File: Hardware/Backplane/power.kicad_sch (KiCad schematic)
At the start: 59 parts, among them J2901 Conn_01x05, U2901 P2X8C4M64P, U2902 AP3445LW6-7

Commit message: Adjusts to review comments
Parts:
- C2901: footprint (none) -> Capacitor_SMD:C_1206_3216Metric; Digikey Part No (none) -> 490-13970-1-ND
- C2902, C2903, C2904, C2905, C2906, C2907, C2908, C2909, C2910, C2911, C2912, C2913, C2914, C2915, C2916, C2917, C2918, C2919, C2920, C2921, C2922, C2923, C2924, C2925, C2926, C2927, C2928, C2929, C2930, C2931, C2932, C2933, C2934: Digikey Part No (none) -> 399-C0603C104M4RACTUCT-ND
- C2935: footprint (none) -> Capacitor_SMD:C_0603_1608Metric; Digikey Part No (none) -> 1276-1070-1-ND
- C2936, C2937: footprint (none) -> Capacitor_SMD:C_0603_1608Metric; Digikey Part No (none) -> 1276-1274-1-ND
- F2901, F2902, F2903: value SMD1206B050TF/15 -> 0ZCF0400FF2A; footprint (none) -> Fuse:Fuse_2920_7451Metric; Digikey Part No 13-SMD1206B050TF/15TR-ND -> 5923-0ZCF0400FF2ACT-ND
- R2901: Digikey Part No (none) -> RR08P75.0KDCT-ND
- R2902: Digikey Part No (none) -> P36KDBCT-ND
- R2903, R2904, R2905, R2906: Digikey Part No (none) -> 311-0.0GRCT-ND

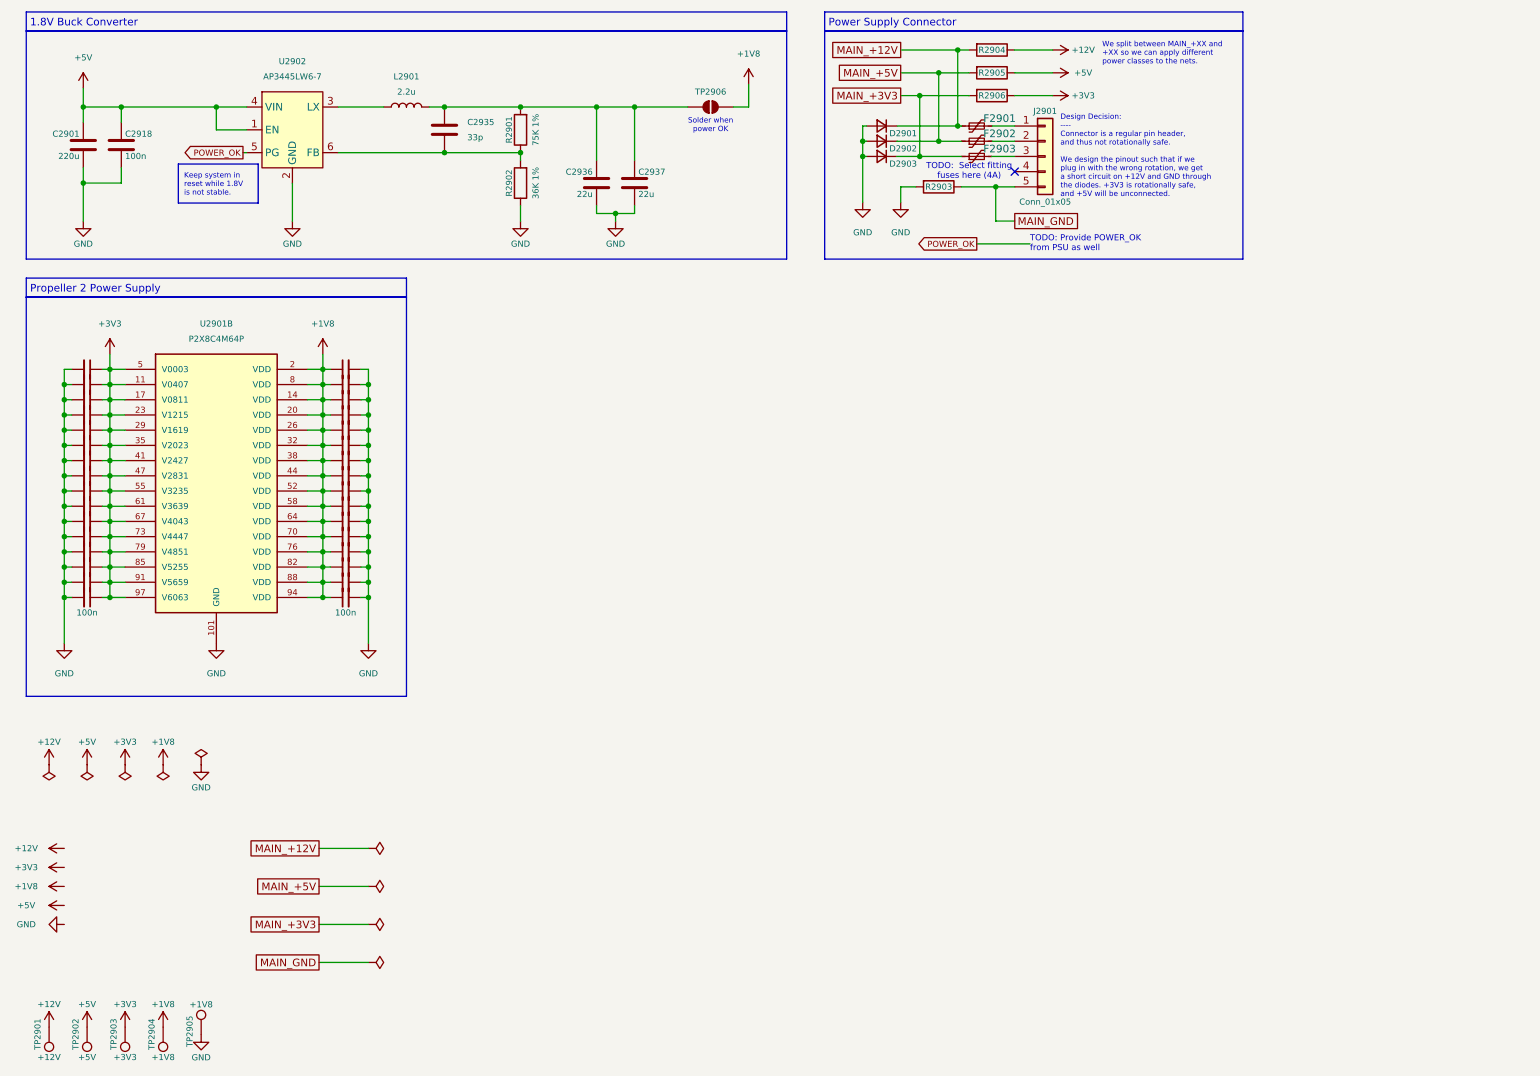
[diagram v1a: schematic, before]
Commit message: Cleans up power connector.
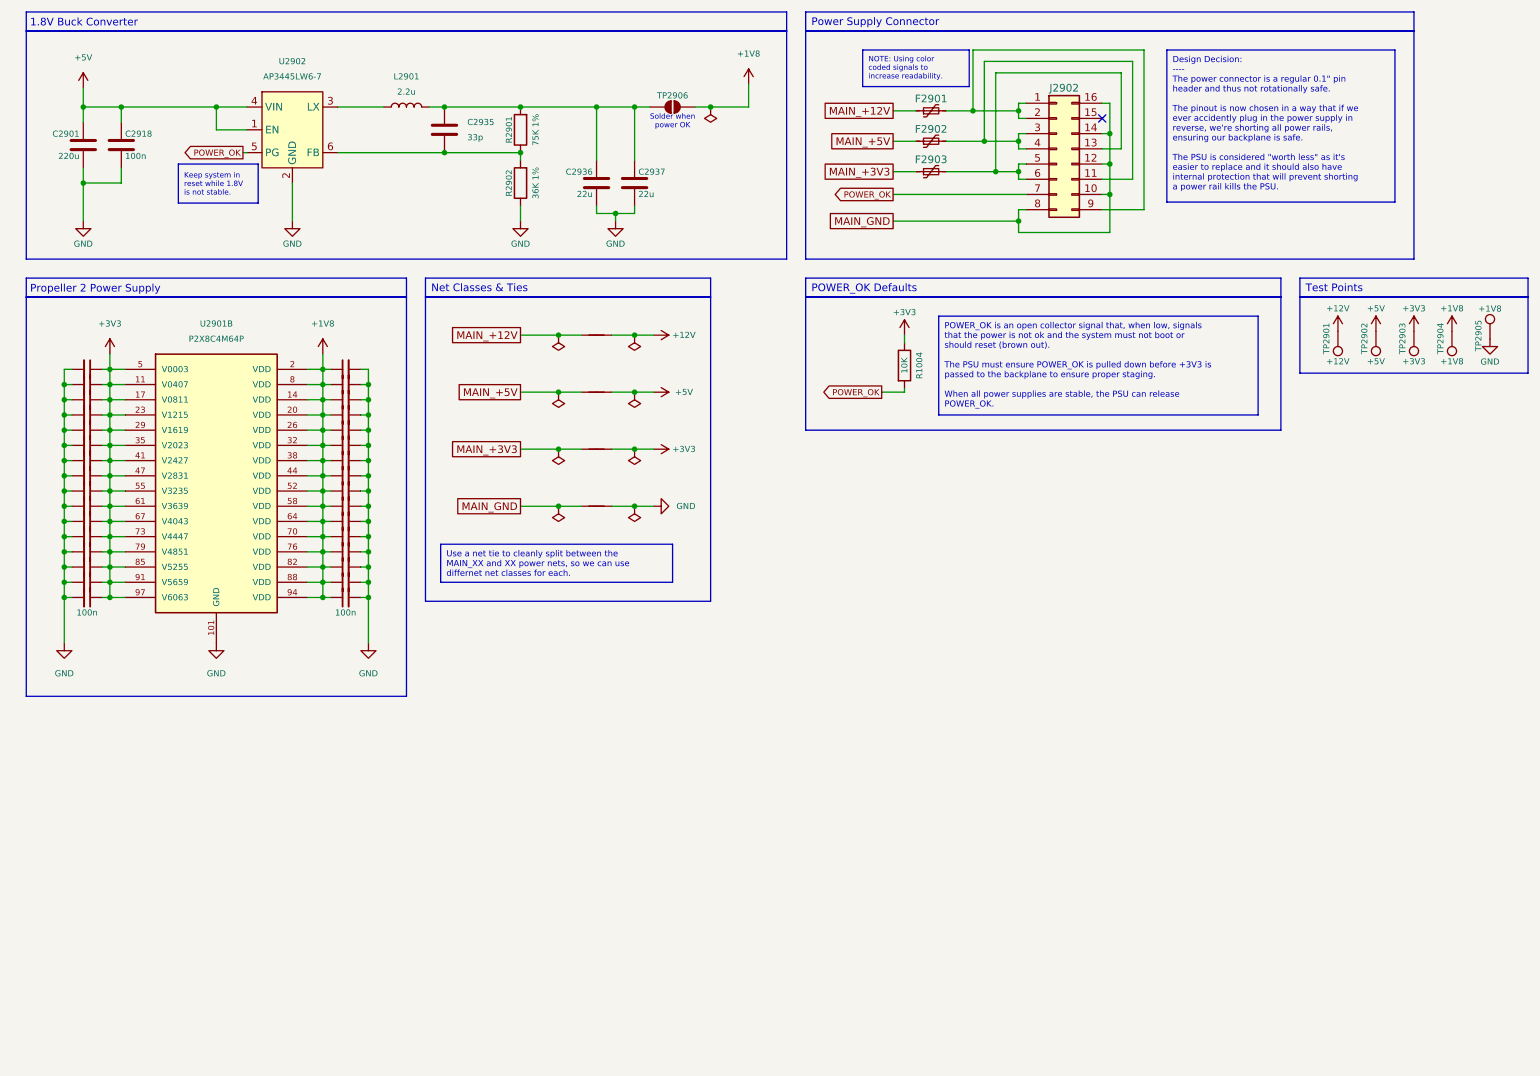
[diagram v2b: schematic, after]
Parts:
- removed D2901, D2902, D2903: Something Short-Circuit Safe, Diode_SMD:D_1206_3216Metric, symbol Device:D_Small
- removed J2901: Conn_01x05, Connector_Phoenix_MC:PhoenixContact_MCV_1,5_5-G-3.5_1x05_P3.50mm_Vertical, symbol Connector_Generic:Conn_01x05
- removed R2903, R2904, R2905, R2906: 0, Resistor_SMD:R_0603_1608Metric, symbol Device:R
- added J2902: Conn_02x08_Counter_Clockwise, symbol Connector_Generic:Conn_02x08_Counter_Clockwise
- added NT2904, NT2905, NT2906, NT2907: NetTie_2, NetTie:NetTie-2_SMD_Pad0.5mm, symbol Device:NetTie_2
- added R1004: 10K, Resistor_SMD:R_0603_1608Metric, symbol Device:R
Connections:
- net +12V: now also NT2905.2
- net +3V3: now also NT2907.2, R1004.1
- net +5V: now also NT2906.2
- net GND: now also NT2904.2
- net MAIN_+12V: now also NT2905.1
- net MAIN_+3V3: now also NT2907.1
- net MAIN_+5V: now also NT2906.1
- net MAIN_GND: now also J2902.10 (Pin_10), J2902.12 (Pin_12), J2902.14 (Pin_14), J2902.16 (Pin_16), J2902.8 (Pin_8), NT2904.1
- net POWER_OK: now also J2902.7 (Pin_7), R1004.2
- net at F2903.2: now also J2902.13 (Pin_13), J2902.5 (Pin_5), J2902.6 (Pin_6)
- net at F2901.2: now also J2902.1 (Pin_1), J2902.2 (Pin_2), J2902.9 (Pin_9)
- net at F2902.2: now also J2902.11 (Pin_11), J2902.3 (Pin_3), J2902.4 (Pin_4)
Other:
- note removed: "Design Decision: ---- Connector is a regular pin header, and thus not rotationally safe. We design the pinout such that if we plug in with the wrong rotation, we get a short circuit on +12V and GND through the diodes. +3V3 is rotationally safe, and +5V will be unconnected."
- note removed: "Power Supply Connector"
- note removed: "TODO: Provide POWER_OK from PSU as well"
- note removed: "TODO: Select fitting fuses here (4A)"
- note removed: "We split between MAIN_+XX and +XX so we can apply different power classes to the nets."
- moved on the sheet: F2901, TP2901, TP2902, TP2903, TP2904, TP2905, TP2906

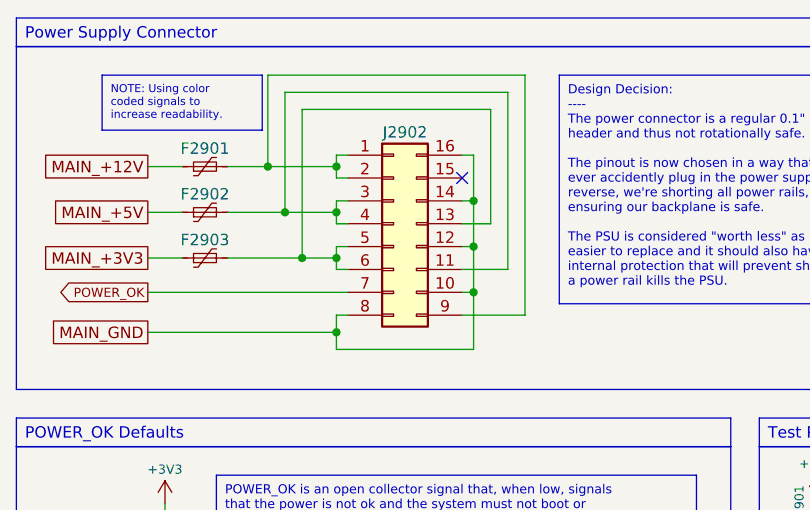
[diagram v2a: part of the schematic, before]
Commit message: Cleans up schematic even more, consolidates 270 and 100 Ohm resistors into the 560 ohm resistor, as they were only used as series resistors for the mosfets and LED current limiters
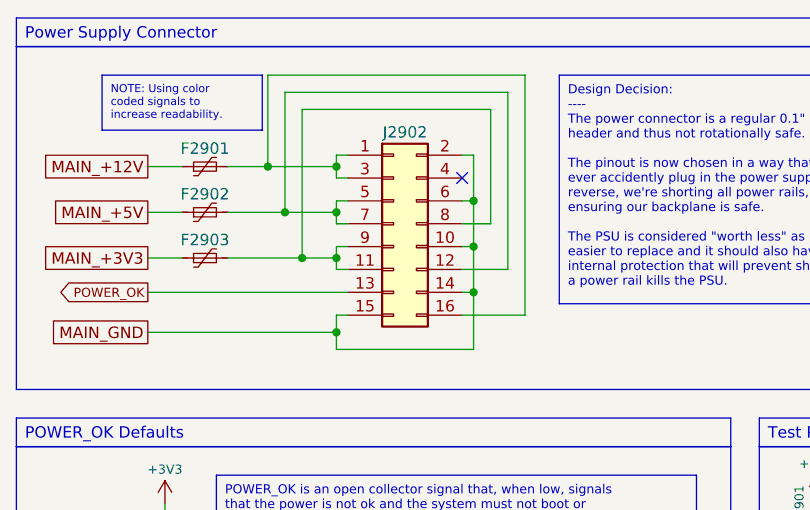
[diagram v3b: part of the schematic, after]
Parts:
- J2902: footprint (none) -> Connector_PinHeader_2.54mm:PinHeader_1x16_P2.54mm_Vertical_SMD_Pin1Left; symbol Connector_Generic:Conn_02x08_Counter_Clockwise -> Connector_Generic:Conn_02x08_Odd_Even
- U2902: footprint (none) -> Package_TO_SOT_SMD:SOT-23-6
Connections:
- net MAIN_GND: now also J2902.15 (Pin_15), J2902.2 (Pin_2), J2902.6 (Pin_6); no longer J2902.12 (Pin_12), J2902.16 (Pin_16), J2902.8 (Pin_8)
- net POWER_OK: now also J2902.13 (Pin_13); no longer J2902.7 (Pin_7)
- net at F2901.2, J2902.1 (Pin_1): now also J2902.16 (Pin_16), J2902.3 (Pin_3); no longer J2902.2 (Pin_2), J2902.9 (Pin_9)
- new net: F2903.2, J2902.11 (Pin_11), J2902.8 (Pin_8), J2902.9 (Pin_9)
- new net: F2902.2, J2902.12 (Pin_12), J2902.5 (Pin_5), J2902.7 (Pin_7)
- now unconnected: J2902.4 (Pin_4)
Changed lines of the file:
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@@
 	)
 	(symbol
-		(lib_id "Connector_Generic:Conn_02x08_Counter_Clockwise")
+		(lib_id "Connector_Generic:Conn_02x08_Odd_Even")
 		(at 191.135 41.91 0)
 		(unit 1)
@@
 			)
 		)
-		(property "Footprint" ""
+		(property "Footprint" "Connector_PinHeader_2.54mm:PinHeader_1x16_P2.54mm_Vertical_SMD_Pin1Left"
 			(at 191.135 41.91 0)
 			(effects
@@
 			)
 		)
-		(property "Description" "Generic connector, double row, 02x08, counter clockwise pin numbering scheme (similar to DIP package numbering), script generated (kicad-library-utils/schlib/autogen/connector/)"
+		(property "Description" "Generic connector, double row, 02x08, odd/even pin numbering scheme (row 1 odd numbers, row 2 even numbers), script generated (kicad-library-utils/schlib/autogen/connector/)"
 			(at 191.135 41.91 0)
 			(effects
@@
 			)
 		)
-		(property "Footprint" ""
+		(property "Footprint" "Package_TO_SOT_SMD:SOT-23-6"
 			(at 63.5 38.735 0)
 			(effects

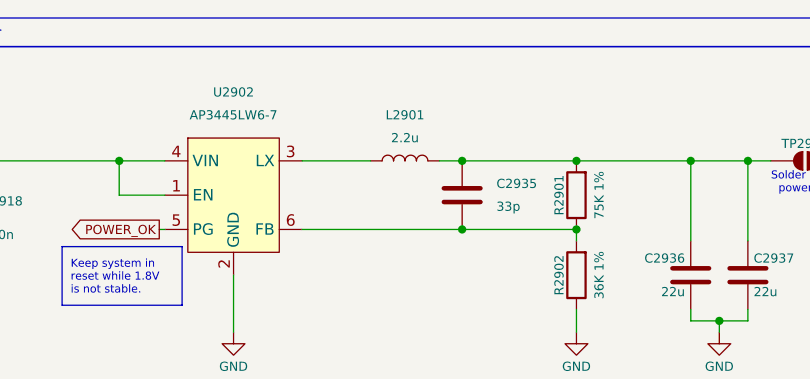
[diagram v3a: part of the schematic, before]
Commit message: More BOM consolidation
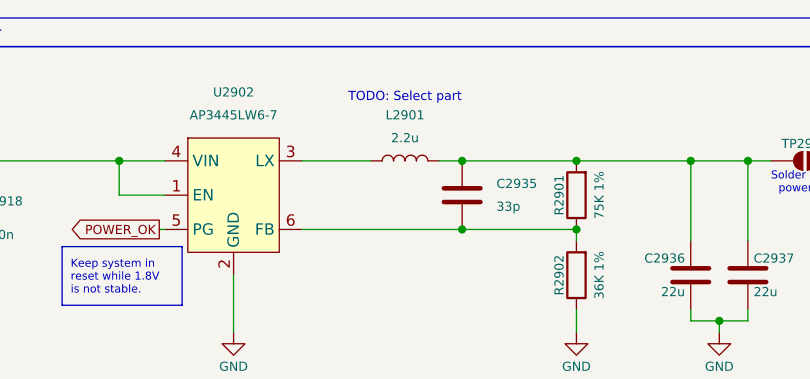
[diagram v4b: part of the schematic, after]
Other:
- note added: "TODO: Select part"
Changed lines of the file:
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@@
+		)
+	)
+	(text "TODO: Select part"
+		(exclude_from_sim no)
+		(at 82.55 27.94 0)
+		(effects
+			(font
+				(size 1.016 1.016)
+			)
 		)
 	)

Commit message: Further backplane PCB cleanup.
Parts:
- J2902: footprint Connector_PinHeader_2.54mm:PinHeader_1x16_P2.54mm_Vertical_SMD_Pin1Left -> Connector_PinHeader_2.54mm:PinHeader_2x08_P2.54mm_Vertical_SMD
- L2901: footprint (none) -> Inductor_SMD:L_1008_2520Metric; Digikey Part No (none) -> 3526-WIP252012S-2R2MLDGCT-ND
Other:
- note removed: "TODO: Select part"
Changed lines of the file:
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@@
 		)
 	)
-	(text "TODO: Select part"
-		(exclude_from_sim no)
-		(at 82.55 27.94 0)
-		(effects
-			(font
-				(size 1.016 1.016)
-			)
-		)
-	)
 	(text_box "NOTE: Using color coded signals to increase readability."
 		(exclude_from_sim no)
@@
 			)
 		)
-		(property "Footprint" "Connector_PinHeader_2.54mm:PinHeader_1x16_P2.54mm_Vertical_SMD_Pin1Left"
+		(property "Footprint" "Connector_PinHeader_2.54mm:PinHeader_2x08_P2.54mm_Vertical_SMD"
 			(at 191.135 41.91 0)
 			(hide yes)
@@
 			)
 		)
-		(property "Footprint" ""
+		(property "Footprint" "Inductor_SMD:L_1008_2520Metric"
 			(at 82.55 34.925 0)
 			(hide yes)
@@
 			)
 		)
-		(property "Datasheet" ""
+		(property "Datasheet" "https://mm.digikey.com/Volume0/opasdata/d220001/medias/docus/8884/3526_WIP252012S%20L%20Series.pdf"
+			(at 82.55 34.925 0)
+			(hide yes)
+			(show_name no)
+			(do_not_autoplace no)
+			(effects
+				(font
+					(size 1.27 1.27)
+				)
+			)
+		)
+		(property "Description" "2.2 µH Shielded Wirewound Inductor 2.2 A 89mOhm Max 1008 (2520 Metric)"
 			(at 82.55 34.925 0)
 			(hide yes)
@@
 			)
 		)
-		(property "Description" "Inductor"
+		(property "Digikey Part No" "3526-WIP252012S-2R2MLDGCT-ND"
 			(at 82.55 34.925 0)
 			(hide yes)

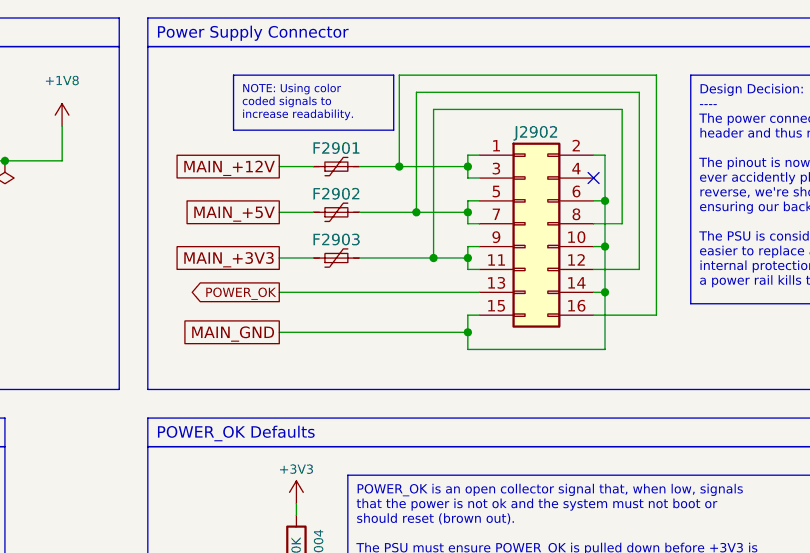
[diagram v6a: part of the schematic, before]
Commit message: Backplane: Fixes missing footprints/parts, starts to work on the layout seriously.
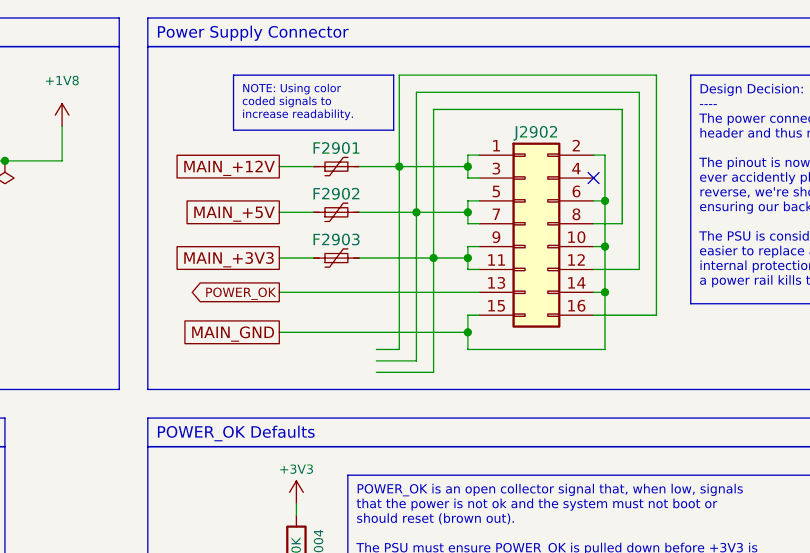
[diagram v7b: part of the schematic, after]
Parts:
- F2901, F2902, F2903: footprint Fuse:Fuse_2920_7451Metric -> Home Computer:FUSER_0ZCF0400FF2A
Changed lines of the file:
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@@
 	(wire
 		(pts
+			(xy 174.625 57.15) (xy 179.07 57.15)
+		)
+		(stroke
+			(width 0)
+			(type default)
+			(color 0 132 132 1)
+		)
+	)
+	(wire
+		(pts
 			(xy 172.72 45.72) (xy 180.975 45.72)
 		)
@@
 	(wire
 		(pts
+			(xy 180.975 45.72) (xy 180.975 58.42)
+		)
+		(stroke
+			(width 0)
+			(type default)
+			(color 132 0 132 1)
+		)
+	)
+	(wire
+		(pts
 			(xy 26.67 109.22) (xy 25.4 109.22)
 		)
@@
 	(wire
 		(pts
+			(xy 177.165 35.56) (xy 177.165 55.88)
+		)
+		(stroke
+			(width 0)
+			(type default)
+			(color 204 102 0 1)
+		)
+	)
+	(wire
+		(pts
 			(xy 107.95 101.6) (xy 111.76 101.6)
 		)
@@
 	(wire
 		(pts
+			(xy 174.625 58.42) (xy 180.975 58.42)
+		)
+		(stroke
+			(width 0)
+			(type default)
+			(color 132 0 132 1)
+		)
+	)
+	(wire
+		(pts
 			(xy 74.93 114.3) (xy 76.2 114.3)
 		)
@@
 	(wire
 		(pts
+			(xy 174.625 55.88) (xy 177.165 55.88)
+		)
+		(stroke
+			(width 0)
+			(type default)
+			(color 204 102 0 1)
+		)
+	)
+	(wire
+		(pts
 			(xy 50.8 38.735) (xy 50.8 34.925)
 		)
@@
 	(wire
 		(pts
+			(xy 179.07 40.64) (xy 179.07 57.15)
+		)
+		(stroke
+			(width 0)
+			(type default)
+			(color 0 132 132 1)
+		)
+	)
+	(wire
+		(pts
 			(xy 74.93 111.76) (xy 76.2 111.76)
 		)
@@
 		(length 2.54)
 		(shape round)
+		(at 174.625 57.15 90)
+		(effects
+			(font
+				(size 1.016 1.016)
+			)
+			(justify left bottom)
+		)
+		(property "Net Class" "Power_4A"
+			(at 171.45 57.15 0)
+			(show_name no)
+			(do_not_autoplace no)
+			(effects
+				(font
+					(size 1.016 1.016)
+					(italic yes)
+				)
+				(justify right)
+			)
+		)
+	)
+	(netclass_flag ""
+		(length 2.54)
+		(shape round)
+		(at 174.625 58.42 90)
+		(effects
+			(font
+				(size 1.016 1.016)
+			)
+			(justify left bottom)
+		)
+		(property "Net Class" "Power_4A"
+			(at 171.45 58.42 0)
+			(show_name no)
+			(do_not_autoplace no)
+			(effects
+				(font
+					(size 1.016 1.016)
+					(italic yes)
+				)
+				(justify right)
+			)
+		)
+	)
+	(netclass_flag ""
+		(length 2.54)
+		(shape round)
 		(at 107.95 101.6 0)
 		(effects
@@
 		(length 2.54)
 		(shape round)
+		(at 174.625 55.88 90)
+		(effects
+			(font
+				(size 1.016 1.016)
+			)
+			(justify left bottom)
+		)
+		(property "Net Class" "Power_4A"
+			(at 171.45 55.88 0)
+			(show_name no)
+			(do_not_autoplace no)
+			(effects
+				(font
+					(size 1.016 1.016)
+					(italic yes)
+				)
+				(justify right)
+			)
+		)
+	)
+	(netclass_flag ""
+		(length 2.54)
+		(shape round)
 		(at 120.65 92.075 0)
 		(effects
@@
 			)
 		)
-		(property "Footprint" "Fuse:Fuse_2920_7451Metric"
+		(property "Footprint" "Home Computer:FUSER_0ZCF0400FF2A"
 			(at 170.18 40.64 0)
 			(hide yes)
@@
 			)
 		)
-		(property "Footprint" "Fuse:Fuse_2920_7451Metric"
+		(property "Footprint" "Home Computer:FUSER_0ZCF0400FF2A"
 			(at 170.18 35.56 0)
 			(hide yes)
@@
 			)
 		)
-		(property "Footprint" "Fuse:Fuse_2920_7451Metric"
+		(property "Footprint" "Home Computer:FUSER_0ZCF0400FF2A"
 			(at 170.18 45.72 0)
 			(hide yes)
